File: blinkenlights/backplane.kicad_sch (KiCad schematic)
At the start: 10 parts, among them J201 Conn_03x32_Row_Letter_First

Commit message: Start work on blinkenlights pcb
- This is mostly for the general layout and physical size of the board;
  all the components are placed on the back so the pin numbers will line
  up properly on the DIN connectors.
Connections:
- net GND: now also J201.a23 (Pin_a23)
- net CLK: now reaches J201.a24 (Pin_a24)
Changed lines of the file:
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@@
 (kicad_sch (version 20210621) (generator eeschema)
   (paper "A4")
+  (junction (at 260.35 19.05) (diameter 0) (color 0 0 0 0))
   (junction (at 207.01 153.67) (diameter 0) (color 0 0 0 0))
+  (junction (at 248.285 153.67) (diameter 0) (color 0 0 0 0))
+  (junction (at 218.44 153.67) (diameter 0) (color 0 0 0 0))
+  (junction (at 224.155 21.59) (diameter 0) (color 0 0 0 0))
+  (junction (at 259.715 158.75) (diameter 0) (color 0 0 0 0))
+  (junction (at 248.285 158.75) (diameter 0) (color 0 0 0 0))
+  (junction (at 224.155 49.53) (diameter 0) (color 0 0 0 0))
+  (junction (at 207.01 158.75) (diameter 0) (color 0 0 0 0))
+  (junction (at 211.455 19.05) (diameter 0) (color 0 0 0 0))
+  (junction (at 224.155 95.25) (diameter 0) (color 0 0 0 0))
   (junction (at 218.44 158.75) (diameter 0) (color 0 0 0 0))
-  (junction (at 224.155 49.53) (diameter 0) (color 0 0 0 0))
-  (junction (at 224.155 95.25) (diameter 0) (color 0 0 0 0))
+  (junction (at 211.455 29.21) (diameter 0) (color 0 0 0 0))
   (junction (at 259.715 153.67) (diameter 0) (color 0 0 0 0))
-  (junction (at 260.35 19.05) (diameter 0) (color 0 0 0 0))
-  (junction (at 211.455 29.21) (diameter 0) (color 0 0 0 0))
-  (junction (at 211.455 19.05) (diameter 0) (color 0 0 0 0))
-  (junction (at 259.715 158.75) (diameter 0) (color 0 0 0 0))
-  (junction (at 218.44 153.67) (diameter 0) (color 0 0 0 0))
-  (junction (at 248.285 158.75) (diameter 0) (color 0 0 0 0))
-  (junction (at 207.01 158.75) (diameter 0) (color 0 0 0 0))
-  (junction (at 248.285 153.67) (diameter 0) (color 0 0 0 0))
-  (junction (at 224.155 21.59) (diameter 0) (color 0 0 0 0))
   (bus_entry (at 230.505 29.21) (size 2.54 -2.54)
     (stroke (width 0) (type default) (color 0 0 0 0))
@@
   )
   (wire (pts (xy 224.155 57.15) (xy 230.505 57.15))
+    (stroke (width 0) (type default) (color 0 0 0 0))
+  )
+  (wire (pts (xy 210.185 77.47) (xy 211.455 77.47))
     (stroke (width 0) (type default) (color 0 0 0 0))
   )
@@
   )
   (hierarchical_label "A{1..23}" (shape bidirectional) (at 202.565 69.85 270)
+    (effects (font (size 1.27 1.27)) (justify right))
+  )
+  (hierarchical_label "CLK" (shape output) (at 210.185 77.47 180)
     (effects (font (size 1.27 1.27)) (justify right))
   )
@@
       (effects (font (size 1.27 1.27)) hide)
     )
+    (pin "1")
+  )
+  (symbol (lib_id "power:GND") (at 211.455 74.93 270) (unit 1)
+    (in_bom yes) (on_board yes) (fields_autoplaced)
+    (property "Reference" "#PWR0225" (id 0) (at 205.105 74.93 0)
+      (effects (font (size 1.27 1.27)) hide)
+    )
+    (property "Value" "GND" (id 1) (at 208.28 75.409 90)
+      (effects (font (size 1.27 1.27)) (justify right))
+    )
+    (property "Footprint" "" (id 2) (at 211.455 74.93 0)
+      (effects (font (size 1.27 1.27)) hide)
+    )
+    (property "Datasheet" "" (id 3) (at 211.455 74.93 0)
+      (effects (font (size 1.27 1.27)) hide)
+    )

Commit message: Added ROM sockets to blinkenlights
- Also started routing some of the IOs and powers for the displays
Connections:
- net +12V: now also F202.2; no longer F202.1
- net +5V: now also F201.2; no longer F201.1
- net at J201.a1 (Pin_a1), J201.a2 (Pin_a2): now also F201.1; no longer F201.2
- net at J201.c1 (Pin_c1), J201.c2 (Pin_c2): now also F202.1; no longer F202.2
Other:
- moved on the sheet: F201, F202
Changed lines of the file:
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@@
-(kicad_sch (version 20210621) (generator eeschema)
+(kicad_sch (version 20211123) (generator eeschema)
   (paper "A4")
-  (junction (at 260.35 19.05) (diameter 0) (color 0 0 0 0))
-  (junction (at 207.01 153.67) (diameter 0) (color 0 0 0 0))
-  (junction (at 248.285 153.67) (diameter 0) (color 0 0 0 0))
-  (junction (at 218.44 153.67) (diameter 0) (color 0 0 0 0))
-  (junction (at 224.155 21.59) (diameter 0) (color 0 0 0 0))
-  (junction (at 259.715 158.75) (diameter 0) (color 0 0 0 0))
-  (junction (at 248.285 158.75) (diameter 0) (color 0 0 0 0))
-  (junction (at 224.155 49.53) (diameter 0) (color 0 0 0 0))
-  (junction (at 207.01 158.75) (diameter 0) (color 0 0 0 0))
-  (junction (at 211.455 19.05) (diameter 0) (color 0 0 0 0))
-  (junction (at 224.155 95.25) (diameter 0) (color 0 0 0 0))
-  (junction (at 218.44 158.75) (diameter 0) (color 0 0 0 0))
-  (junction (at 211.455 29.21) (diameter 0) (color 0 0 0 0))
-  (junction (at 259.715 153.67) (diameter 0) (color 0 0 0 0))
+  (junction (at 207.01 158.75) (diameter 0) (color 0 0 0 0)
+  )
+  (junction (at 248.285 153.67) (diameter 0) (color 0 0 0 0)
+  )
+  (junction (at 248.285 158.75) (diameter 0) (color 0 0 0 0)
+  )
+  (junction (at 207.01 153.67) (diameter 0) (color 0 0 0 0)
+  )
+  (junction (at 224.155 21.59) (diameter 0) (color 0 0 0 0)
+  )
+  (junction (at 224.155 49.53) (diameter 0) (color 0 0 0 0)
+  )
+  (junction (at 211.455 29.21) (diameter 0) (color 0 0 0 0)
+  )
+  (junction (at 218.44 153.67) (diameter 0) (color 0 0 0 0)
+  )
+  (junction (at 259.715 158.75) (diameter 0) (color 0 0 0 0)
+  )
+  (junction (at 218.44 158.75) (diameter 0) (color 0 0 0 0)
+  )
+  (junction (at 224.155 95.25) (diameter 0) (color 0 0 0 0)
+  )
+  (junction (at 211.455 19.05) (diameter 0) (color 0 0 0 0)
+  )
+  (junction (at 259.715 153.67) (diameter 0) (color 0 0 0 0)
+  )
+  (junction (at 260.35 19.05) (diameter 0) (color 0 0 0 0)
+  )
   (bus_entry (at 230.505 29.21) (size 2.54 -2.54)
     (stroke (width 0) (type default) (color 0 0 0 0))
@@
     (pin "b9")
   )
-  (symbol (lib_id "Device:Polyfuse_Small") (at 201.295 19.05 90) (unit 1)
-    (in_bom yes) (on_board yes) (fields_autoplaced)
-    (property "Reference" "F201" (id 0) (at 201.295 14.1945 90))
-    (property "Value" "1.5A" (id 1) (at 201.295 16.9696 90))
-    (property "Footprint" "Fuse:Fuse_Bourns_MF-SM_7.98x5.44mm" (id 2) (at 206.375 17.78 0)
+  (symbol (lib_id "Device:Polyfuse_Small") (at 201.295 19.05 270) (mirror x) (unit 1)
+    (in_bom yes) (on_board yes) (fields_autoplaced)
+    (property "Reference" "F201" (id 0) (at 201.295 13.335 90))
+    (property "Value" "1.5A" (id 1) (at 201.295 15.875 90))
+    (property "Footprint" "Fuse:Fuse_Bourns_MF-SM_7.98x5.44mm" (id 2) (at 196.215 17.78 0)
       (effects (font (size 1.27 1.27)) (justify left) hide)
     )
@@
     (pin "2")
   )
-  (symbol (lib_id "Device:Polyfuse_Small") (at 249.555 19.05 90) (unit 1)
-    (in_bom yes) (on_board yes) (fields_autoplaced)
-    (property "Reference" "F202" (id 0) (at 249.555 14.1945 90))
-    (property "Value" ".5A" (id 1) (at 249.555 16.9696 90))
-    (property "Footprint" "Fuse:Fuse_Littelfuse-NANO2-451_453" (id 2) (at 254.635 17.78 0)
+  (symbol (lib_id "Device:Polyfuse_Small") (at 249.555 19.05 270) (mirror x) (unit 1)
+    (in_bom yes) (on_board yes)
+    (property "Reference" "F202" (id 0) (at 249.555 13.335 90))
+    (property "Value" ".5A" (id 1) (at 249.555 15.875 90))
+    (property "Footprint" "Fuse:Fuse_Littelfuse-NANO2-451_453" (id 2) (at 244.475 17.78 0)
       (effects (font (size 1.27 1.27)) (justify left) hide)
     )

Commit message: Reworked blinkenlights board
- The connector for the CPU board is a female vertical DIN connector
  instead now, which will be a lot less fucky

- Some more LEDs and buttons
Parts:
- J201: footprint Connector_DIN:DIN41612_R_3x32_Male_Horizontal_THT -> Connector_DIN:DIN41612_C_3x32_Female_Vertical_THT
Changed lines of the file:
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@@
     (property "Reference" "J201" (id 0) (at 217.805 13.8135 0))
     (property "Value" "Conn_03x32_Row_Letter_First" (id 1) (at 217.805 16.5886 0))
-    (property "Footprint" "Connector_DIN:DIN41612_R_3x32_Male_Horizontal_THT" (id 2) (at 216.535 57.15 0)
+    (property "Footprint" "Connector_DIN:DIN41612_C_3x32_Female_Vertical_THT" (id 2) (at 216.535 57.15 0)
       (effects (font (size 1.27 1.27)) hide)
     )
@@
       (effects (font (size 1.27 1.27)) (justify right))
     )
-    (property "Footprint" "Connector_DIN:DIN41612_R_3x32_Male_Horizontal_THT" (id 2) (at 267.97 57.15 0)
-      (effects (font (size 1.27 1.27)) hide)
-    )
+    (property "Footprint" "Connector_DIN:DIN41612_C_3x32_Female_Vertical_THT" (id 2) (at 267.97 57.15 0)
+      (effects (font (size 1.27 1.27)) hide)
+    )

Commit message: Rework blinkenlights board
- Removed ROMs, GALs and so forth from the blinkenlights board and
  simplified the power distribution significantly. This is in
  preparation for simply placing a big ass microcontroller that allows
  us to perform bus transactions manually (to load bootstrap programs,
  for example) on the system.
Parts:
- added TP202: TestPoint, TestPoint:TestPoint_Loop_D2.60mm_Drill1.4mm_Beaded, symbol Connector:TestPoint
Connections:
- net CLK: now also TP202.1
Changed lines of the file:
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@@
+    (stroke (width 0) (type default) (color 0 0 0 0))
+  )
+  (wire (pts (xy 254.635 111.76) (xy 264.795 111.76))
     (stroke (width 0) (type default) (color 0 0 0 0))
   )
@@
   (label "A11" (at 211.455 62.23 180)
     (effects (font (size 1.27 1.27)) (justify right bottom))
+  )
+  (label "CLK" (at 254.635 111.76 0)
+    (effects (font (size 1.27 1.27)) (justify left bottom))
   )
   (label "A[1..23]" (at 233.045 69.85 0)
@@
       (effects (font (size 1.27 1.27)) hide)
     )
+    (pin "1")
+  )
+  (symbol (lib_id "Connector:TestPoint") (at 264.795 111.76 270) (unit 1)
+    (in_bom yes) (on_board yes)
+    (property "Reference" "TP202" (id 0) (at 269.5702 111.76 90)
+      (effects (font (size 1.27 1.27)) (justify left))
+    )
+    (property "Value" "TestPoint" (id 1) (at 269.5702 112.903 90)
+      (effects (font (size 1.27 1.27)) (justify left) hide)
+    )
+    (property "Footprint" "TestPoint:TestPoint_Loop_D2.60mm_Drill1.4mm_Beaded" (id 2) (at 264.795 116.84 0)
+      (effects (font (size 1.27 1.27)) hide)
+    )
+    (property "Datasheet" "~" (id 3) (at 264.795 116.84 0)
+      (effects (font (size 1.27 1.27)) hide)
+    )
+    (property "MPN" "534-5001" (id 4) (at 264.795 111.76 90)
+      (effects (font (size 1.27 1.27)) hide)
+    )

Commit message: Routed address/data bus on blinkenlights
- It goes to the funky hex display bois now and is routed so that it
  should be pretty ez to yeet on down into level shifters for the big
  ARM chip that runs the show
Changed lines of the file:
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@@
     (effects (font (size 1.27 1.27)) (justify right))
   )
-  (hierarchical_label "D{0..15}" (shape bidirectional) (at 233.045 25.4 0)
+  (hierarchical_label "D[0..15]" (shape bidirectional) (at 233.045 25.4 0)
     (effects (font (size 1.27 1.27)) (justify left))
   )
@@
     (effects (font (size 1.27 1.27)) (justify left))
   )
-  (hierarchical_label "A{1..23}" (shape bidirectional) (at 233.045 46.99 0)
+  (hierarchical_label "A[1..23]" (shape bidirectional) (at 233.045 46.99 0)
     (effects (font (size 1.27 1.27)) (justify left))
   )
@@
     (effects (font (size 1.27 1.27)) (justify left))
   )
-  (hierarchical_label "A{1..23}" (shape bidirectional) (at 251.46 69.85 270)
+  (hierarchical_label "A[1..23]" (shape bidirectional) (at 251.46 69.85 270)
     (effects (font (size 1.27 1.27)) (justify right))
   )
@@
     (effects (font (size 1.27 1.27)) (justify right))
   )
-  (hierarchical_label "D{0..15}" (shape bidirectional) (at 202.565 42.545 180)
+  (hierarchical_label "D[0..15]" (shape bidirectional) (at 202.565 42.545 180)
     (effects (font (size 1.27 1.27)) (justify right))
   )
@@
     (effects (font (size 1.27 1.27)) (justify left))
   )
-  (hierarchical_label "A{1..23}" (shape bidirectional) (at 202.565 69.85 270)
+  (hierarchical_label "A[1..23]" (shape bidirectional) (at 202.565 69.85 270)
     (effects (font (size 1.27 1.27)) (justify right))
   )
@@
     (effects (font (size 1.27 1.27)) (justify right))
   )
-  (hierarchical_label "D{0..15}" (shape bidirectional) (at 251.46 39.37 180)
+  (hierarchical_label "D[0..15]" (shape bidirectional) (at 251.46 39.37 180)
     (effects (font (size 1.27 1.27)) (justify right))
   )

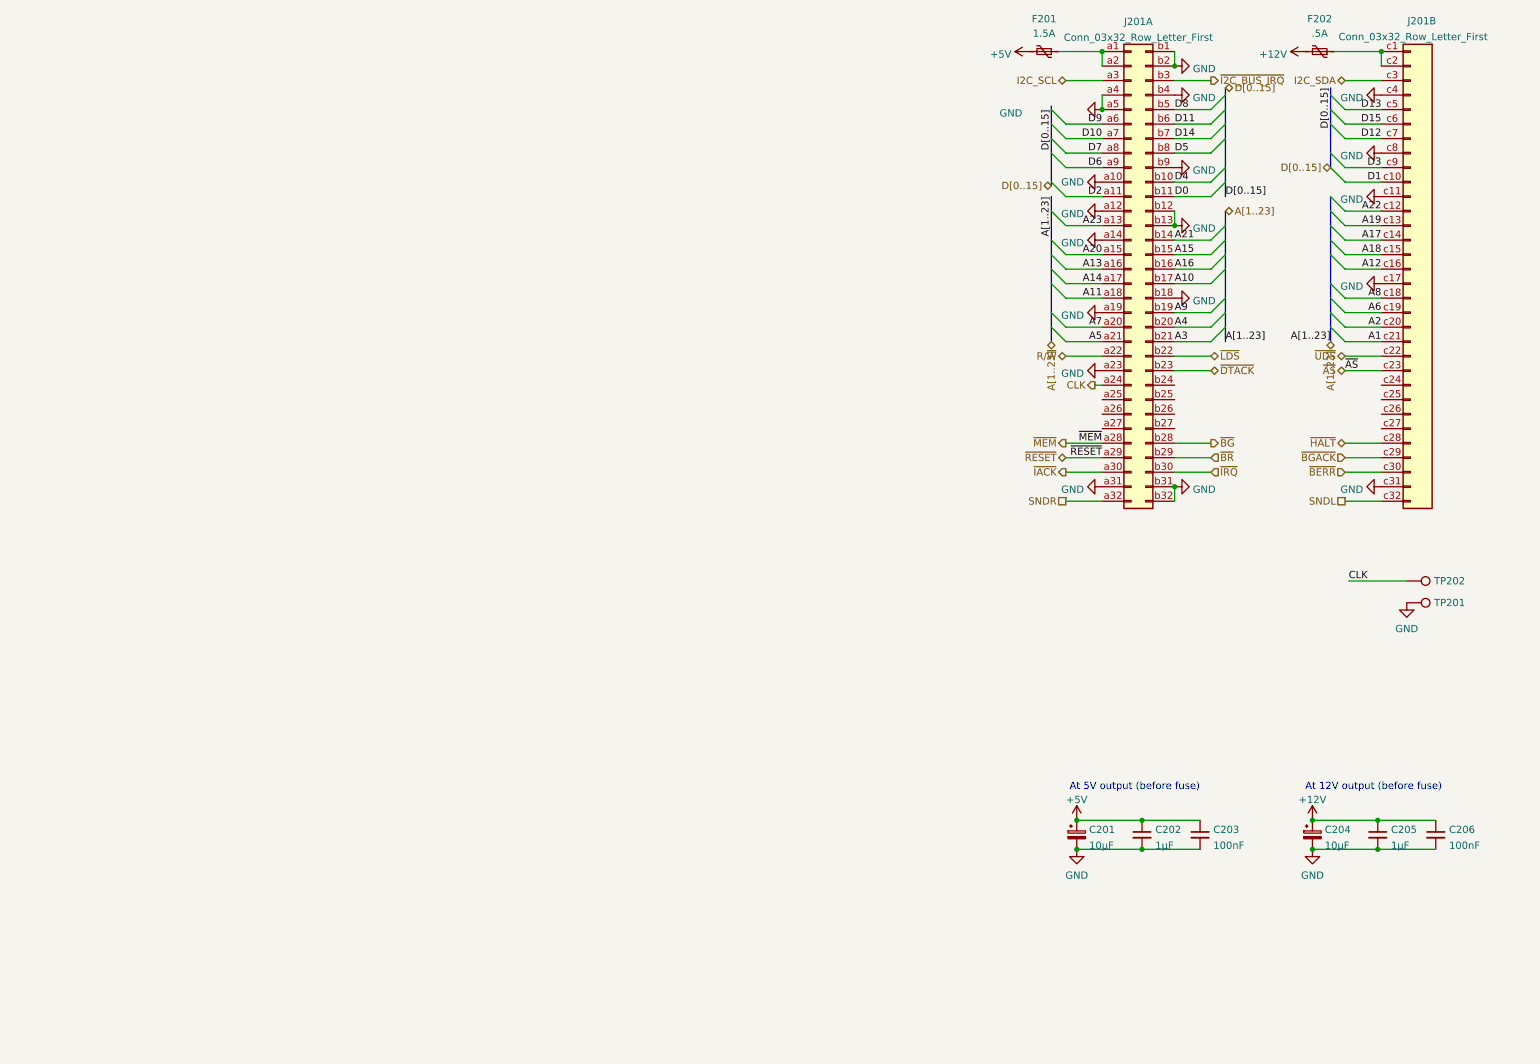
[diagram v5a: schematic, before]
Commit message: Mostly finished blinkenlights contraption
- Added some headers that can have logic probes connected to them; we
  need to route them and ensure the pins are correct
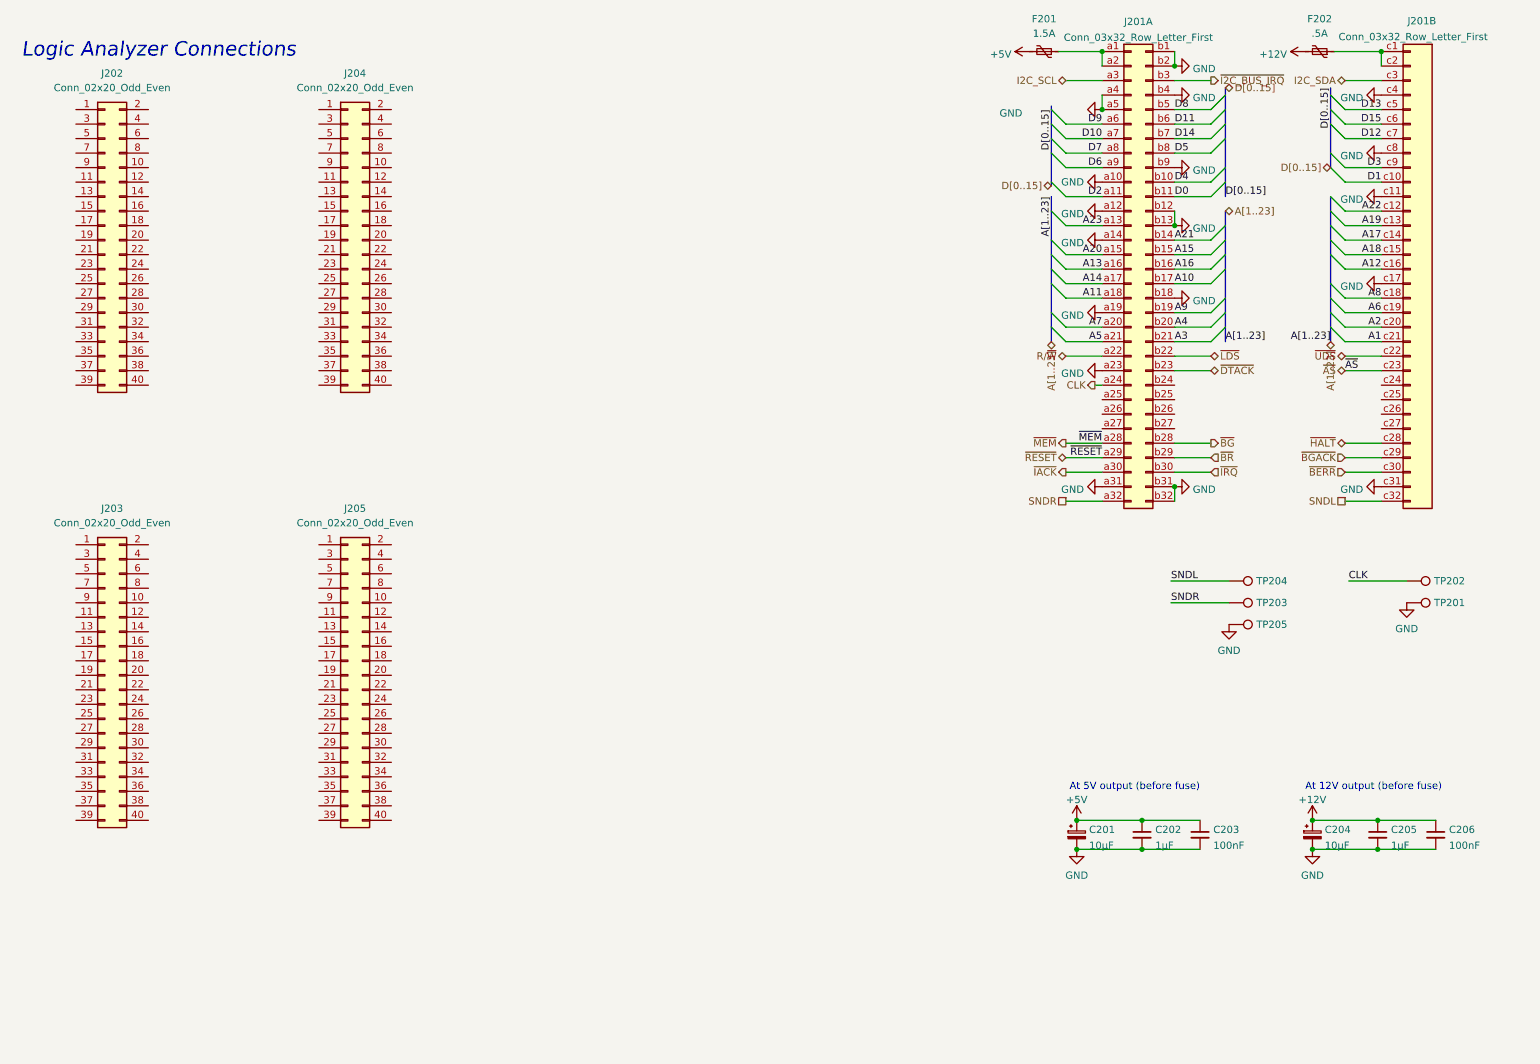
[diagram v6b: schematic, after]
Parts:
- added J202, J203, J204, J205: Conn_02x20_Odd_Even, Connector_PinHeader_2.54mm:PinHeader_2x20_P2.54mm_Vertical, symbol Connector_Generic:Conn_02x20_Odd_Even
- added TP203, TP204, TP205: TestPoint, TestPoint:TestPoint_Loop_D2.60mm_Drill1.4mm_Beaded, symbol Connector:TestPoint
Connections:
- net GND: now also TP205.1
- net SNDL: now also TP204.1
- net SNDR: now also TP203.1
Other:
- note added: "Logic Analyzer Connections"
